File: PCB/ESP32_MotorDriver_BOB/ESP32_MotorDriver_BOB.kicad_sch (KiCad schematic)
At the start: 39 parts, among them J1 USB_C_Receptacle_USB2.0, J2 Conn_01x06, J3 Conn_01x06, J5 Conn_01x18, J6 Conn_01x07, Q1 SSM3J338R_LF, SW1 EN, SW2 BOOT, U1 ESP32-S2-SOLO-N4, U2 D3V3XA4B10LP, U4 TB6612FNG, U5 AP63203WU

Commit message: actual _v01
Issue with files being copied - these should be good
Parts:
- removed C1, C3, C5, C7: 10uF, Capacitor_SMD:C_0805_2012Metric_Pad1.18x1.45mm_HandSolder, symbol Device:C
- removed C10, C9: 22uF, Capacitor_SMD:C_0805_2012Metric_Pad1.18x1.45mm_HandSolder, symbol Device:C
- removed C2, C4, C6, C8: 100nF, Capacitor_SMD:C_0402_1005Metric_Pad0.74x0.62mm_HandSolder, symbol Device:C
- removed D1, D2: D_Schottky, Diode_SMD:D_SOD-323F, symbol Device:D_Schottky
- removed J1: USB_C_Receptacle_USB2.0, Connector_USB:USB_C_Receptacle_HRO_TYPE-C-31-M-12, symbol Connector:USB_C_Receptacle_USB2.0
- removed J2, J3: Conn_01x06, Connector_PinHeader_2.54mm:PinHeader_1x06_P2.54mm_Vertical, symbol Connector_Generic:Conn_01x06
- removed J5: Conn_01x18, Connector_PinHeader_2.54mm:PinHeader_1x18_P2.54mm_Vertical, symbol Connector_Generic:Conn_01x18
- removed L1: 4.7uH, Inductor_SMD:L_1008_2520Metric_Pad1.43x2.20mm_HandSolder, symbol Device:L_Small
- removed U1: ESP32-S2-SOLO-N4, ESP32_S2_SOLO_N4:XCVR_ESP32-S2-SOLO-N4, symbol ESP32-S2-SOLO-N4:ESP32-S2-SOLO-N4
- removed U2: D3V3XA4B10LP, Package_DFN_QFN:Diodes_UDFN-10_1x2.5mm_P0.5mm, symbol Power_Protection:D3V3XA4B10LP
- removed U4: TB6612FNG, Package_SO:SSOP-24_5.3x8.2mm_P0.65mm, symbol Driver_Motor:TB6612FNG
- removed U5: AP63203WU, Package_TO_SOT_SMD:TSOT-23-6, symbol Regulator_Switching:AP63203WU
- added C16: 100nF, Capacitor_SMD:C_0402_1005Metric_Pad0.74x0.62mm_HandSolder, symbol Device:C
- added D1: RED, LED_SMD:LED_1206_3216Metric_Pad1.42x1.75mm_HandSolder, symbol Device:LED
- added D2: GREEN, LED_SMD:LED_1206_3216Metric_Pad1.42x1.75mm_HandSolder, symbol Device:LED
- added D3: BLUE, LED_SMD:LED_1206_3216Metric_Pad1.42x1.75mm_HandSolder, symbol Device:LED
- added D4: YELLOW, LED_SMD:LED_1206_3216Metric_Pad1.42x1.75mm_HandSolder, symbol Device:LED
- added H1, H2, H3, H4: MountingHole, MountingHole:MountingHole_3.2mm_M3, symbol Mechanical:MountingHole
- added J10: Conn_01x07, Connector_PinSocket_2.54mm:PinSocket_1x07_P2.54mm_Vertical, symbol Connector_Generic:Conn_01x07
- added J11, J2: Conn_01x05, Connector_PinSocket_2.54mm:PinSocket_1x05_P2.54mm_Vertical, symbol Connector_Generic:Conn_01x05
- added J12, J4: Conn_01x06, Connector_PinSocket_2.54mm:PinSocket_1x06_P2.54mm_Vertical, symbol Connector_Generic:Conn_01x06
- added J13, J3: Conn_01x17, Connector_PinSocket_2.54mm:PinSocket_1x17_P2.54mm_Vertical, symbol Connector_Generic:Conn_01x17
- added J14: Conn_02x03_Odd_Even, Connector_PinHeader_2.54mm:PinHeader_2x03_P2.54mm_Vertical, symbol Connector_Generic:Conn_02x03_Odd_Even
- added J15: Conn_02x08_Odd_Even, Connector_PinHeader_2.54mm:PinHeader_2x08_P2.54mm_Vertical, symbol Connector_Generic:Conn_02x08_Odd_Even
- added J5, J6: Conn_01x06, Connector_JST:JST_XH_S6B-XH-A_1x06_P2.50mm_Horizontal, symbol Connector_Generic:Conn_01x06
- added J7: XT30, Connector_AMASS:AMASS_XT30PW-M_1x02_P2.50mm_Horizontal, symbol Connector:Conn_01x02_Pin
- added J8, J9: Conn_01x03, Connector_PinHeader_2.54mm:PinHeader_1x03_P2.54mm_Vertical, symbol Connector_Generic:Conn_01x03
- added R13, R14: 10k, Resistor_SMD:R_0402_1005Metric_Pad0.72x0.64mm_HandSolder, symbol Device:R
- added R5: 100k, Resistor_SMD:R_0402_1005Metric_Pad0.72x0.64mm_HandSolder, symbol Device:R
- added R6, R7, R8: 4k7, Resistor_SMD:R_0402_1005Metric_Pad0.72x0.64mm_HandSolder, symbol Device:R
- added U1: LDL1117S50R, Package_TO_SOT_SMD:SOT-223-3_TabPin2, symbol Regulator_Linear:LD1117S50TR_SOT223
- added U2: ER_OLEDM0.91_1x-I2C, Display:ER_OLEDM0.91_1x-I2C, symbol Display_Graphic:ER_OLEDM0.91_1x-I2C
- added U3: PCA9306D, Package_SO:SO-8_3.9x4.9mm_P1.27mm, symbol Interface:PCA9306D
- added U4: ESP32 MotorDriver BOB_v01, _silkscreen:logo_QUT, symbol _silkscreen:logo_qut
- C11: footprint Capacitor_SMD:C_0805_2012Metric_Pad1.18x1.45mm_HandSolder -> Capacitor_SMD:C_0402_1005Metric_Pad0.74x0.62mm_HandSolder; Manufacturer (none) -> Samsung Electro-Mechanics; PN_Digikey (none) -> 1276-CL05A106MP6NUN8CT-ND; PN_LCSC (none) -> C3902158; PN_Manufacturer (none) -> CL05A106MP6NUN8
- C12: Manufacturer (none) -> YAGEO; PN_Digikey (none) -> 311-3342-1-ND; PN_LCSC (none) -> C105882; PN_Manufacturer (none) -> CC0402KRX5R9BB104
- C13: value 100nF -> 10uF; LCSC PN C105882 -> C3902158; Manufacturer (none) -> Samsung Electro-Mechanics; PN_Digikey (none) -> 1276-CL05A106MP6NUN8CT-ND; PN_LCSC (none) -> C3902158; PN_Manufacturer (none) -> CL05A106MP6NUN8
- C14: value 100nF -> 10uF; LCSC PN (none) -> C3902158; Manufacturer (none) -> Samsung Electro-Mechanics; PN_Digikey (none) -> 1276-CL05A106MP6NUN8CT-ND; PN_LCSC (none) -> C3902158; PN_Manufacturer (none) -> CL05A106MP6NUN8
- C15: value 10uF -> 100nF; footprint Capacitor_SMD:C_0805_2012Metric_Pad1.18x1.45mm_HandSolder -> Capacitor_SMD:C_0402_1005Metric_Pad0.74x0.62mm_HandSolder; LCSC PN (none) -> C105882; Manufacturer (none) -> YAGEO; PN_Digikey (none) -> 311-3342-1-ND; PN_LCSC (none) -> C105882; PN_Manufacturer (none) -> CC0402KRX5R9BB104
- F1: footprint Fuse:Fuse_0805_2012Metric_Pad1.15x1.40mm_HandSolder -> digikey-footprints:0805; Manufacturer (none) -> Vishay
- J1: renamed from J6; footprint Connector_PinHeader_2.54mm:PinHeader_1x07_P2.54mm_Vertical -> Connector_PinSocket_2.54mm:PinSocket_1x07_P2.54mm_Vertical
- Q1: footprint SSM3J338R_LF:SOT-23F_TOS -> SSM3J338R:SOT-23F_TOS; Manufacturer (none) -> Toshiba Semiconductor and Storage
- R1, R2: value 5k1 -> 150R
- R10: value 4k7 -> 10k; LCSC PN (none) -> C851816; LCSC Part # C100047 -> (none); Manufacturer (none) -> YAGEO; PN_Digikey (none) -> YAG1249CT-ND; PN_LCSC (none) -> C851816; PN_Manufacturer (none) -> RC0402FR-0710KP
- R11, R12: LCSC PN C851816 -> (none)
- R3, R4: value 10k -> 150R; LCSC Part # C100047 -> (none)
- R9: LCSC Part # C100047 -> (none)
- SW1: value EN -> SW_Push; footprint _common:Switch SMD STO -> Button_Switch_SMD:SW_SPST_EVQP0; PN_Digikey 2508-R-667995CT-ND -> P12966SCT-ND; PN_Manufacturer R-667995 -> (none)
- SW2: value BOOT -> SW_Push; footprint _common:Switch SMD STO -> Button_Switch_SMD:SW_SPST_EVQP0; LCSC_PN C25168823 -> (none); PN_Digikey 2508-R-667995CT-ND -> P12966SCT-ND; PN_Manufacturer R-667995 -> (none)
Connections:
- net BOOT is gone; now on net GND: R4.2, SW2.1
- net EN is gone; now on net GND: R3.2, SW1.1
- net M01_STBY is gone; now on net IO8: R12.2
- net SCL is gone; now on net +3V3: R9.2
- net SDA is gone; now on an unnamed net: R10.2
- net +3V3: now also R11.2, J13.10 (Pin_10), J13.11 (Pin_11), J3.10 (Pin_10), J3.11 (Pin_11), J5.3 (Pin_3), J6.3 (Pin_3), R13.2, R8.2, U3.2 (VREF1); no longer C14.1, R10.1, R3.1, R4.1, R9.1
- net GND: now also C13.2, R1.2, R10.1, R2.2, C16.2, J10.1 (Pin_1), J12.6 (Pin_6), J13.1 (Pin_1), J13.17 (Pin_17), J14.1 (Pin_1), J15.10 (Pin_10), J15.12 (Pin_12), J15.14 (Pin_14), J15.16 (Pin_16), J15.2 (Pin_2), J15.4 (Pin_4), J15.6 (Pin_6), J15.8 (Pin_8), J3.1 (Pin_1), J3.17 (Pin_17), J4.6 (Pin_6), J5.6 (Pin_6), J6.6 (Pin_6), J7.1 (Pin_1), J8.1 (Pin_1), J9.1 (Pin_1), U1.1 (GND), U2.1 (GND), U3.1 (GND); no longer R1.1, R11.1, R12.1, R2.1, SW1.2, SW2.2
- net IO1: now also J13.2 (Pin_2), J3.2 (Pin_2), J8.3 (Pin_3)
- net IO15: now also J10.6 (Pin_6), J15.15 (Pin_15)
- net IO16: now also J10.7 (Pin_7), J15.13 (Pin_13)
- net IO17: now also J11.1 (Pin_1), J15.11 (Pin_11), J2.1 (Pin_1)
- net IO18: now also J11.2 (Pin_2), J15.9 (Pin_9), J2.2 (Pin_2)
- net IO2: now also J13.3 (Pin_3), J3.3 (Pin_3), J9.3 (Pin_3)
- net IO3: now also J11.4 (Pin_4), J2.4 (Pin_4), J5.4 (Pin_4)
- net IO39: now also J13.9 (Pin_9), J15.7 (Pin_7), J3.9 (Pin_9)
- net IO4: now also D1.2 (A), J10.2 (Pin_2)
- net IO40: now also J13.8 (Pin_8), J15.5 (Pin_5), J3.8 (Pin_8)
- net IO41: now also J13.7 (Pin_7), J15.3 (Pin_3), J3.7 (Pin_7)
- net IO42: now also J13.6 (Pin_6), J15.1 (Pin_1), J3.6 (Pin_6)
- net IO5: now also D2.2 (A), J10.3 (Pin_3)
- net IO6: now also D3.2 (A), J10.4 (Pin_4)
- net IO7: now also D4.2 (A), J10.5 (Pin_5)
- net IO8: now also C15.1, J11.3 (Pin_3), J2.3 (Pin_3)
- net IO9: now also J11.5 (Pin_5), J2.5 (Pin_5), J5.5 (Pin_5)
- net M1.1: now also J12.2 (Pin_2), J4.2 (Pin_2), J5.1 (Pin_1)
- net M1.2: now also J12.3 (Pin_3), J4.3 (Pin_3), J5.2 (Pin_2)
- net M2.1: now also J12.5 (Pin_5), J4.5 (Pin_5), J6.1 (Pin_1)
- net M2.2: now also J12.4 (Pin_4), J4.4 (Pin_4), J6.2 (Pin_2)
- net RXD: now also J13.5 (Pin_5), J14.3 (Pin_3), J3.5 (Pin_5)
- net TXD: now also J13.4 (Pin_4), J14.4 (Pin_4), J3.4 (Pin_4)
- net Vbatt: now also C11.1, C12.1, C13.1, F1.2, J12.1 (Pin_1), J4.1 (Pin_1), U1.3 (VI); no longer Q1.2
- net at Q1.1: no longer R11.2
- removed net VM: C11.1, C12.1, C15.1, F1.2
- new net: D2.1 (K), R2.1
- new net: D4.1 (K), R4.1
- new net: R13.1, R14.1, SW2.2
- new net: R11.1, R12.1, SW1.2
- new net: R5.1, U3.8 (EN)
- new net: D3.1 (K), R3.1
- new net: J7.2 (Pin_2), Q1.2
- new net: D1.1 (K), R1.1
- new net +5V: C14.1, J14.2 (Pin_2), J8.2 (Pin_2), J9.2 (Pin_2), R5.2, R6.2, R7.2, U1.2 (VO), U2.2 (VCC), U3.7 (VREF2)
- new net IO11: J13.16 (Pin_16), J3.16 (Pin_16), J6.4 (Pin_4)
- new net IO12: J13.15 (Pin_15), J3.15 (Pin_15), J6.5 (Pin_5)
- new net IO13: C16.1, J13.14 (Pin_14), J3.14 (Pin_14), R14.2
- new net IO33: J13.13 (Pin_13), J3.13 (Pin_13), R9.1, U3.3 (SCL1)
- new net IO34: J13.12 (Pin_12), J3.12 (Pin_12), R8.1, U3.4 (SDA1)
- new net SCL_5V0: J14.6 (Pin_6), R6.1, U2.3 (SCL), U3.6 (SCL2)
- new net SDA_5V0: J14.5 (Pin_5), R7.1, U2.4 (SDA), U3.5 (SDA2)
- no-connect marks 1 -> 0
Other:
- note added: "5V 1.2A for Servos etc"
- note added: "Battery Input and Protection"
- note added: "Four LEDs ( R, G, B, Y )"
- note added: "Header IOs for the ESP32"
- note added: "Header for all comms"
- note added: "I2C pull ups and level shift to 5V0"
- note added: "IO Mapping"
- note added: "Line Follower Strip IO"
- note added: "Most servos can take 3V3 PWM"
- note added: "Motor with encoder connecion via JST-XH"
- note added: "OLED on I2C"
- note added: "Second copy, 100mil away from the ESP32 for adding in wires etc"
- note added: "Switches with hardware debounce"
- note added: "Two Servo Connectors"
- note removed: "ESP32"
- note removed: "ESP32 Pin Swaps SPI.begin(sck, miso, mosi, cs); Wire.begin(I2C_SDA, I2C_SCL);"
- note removed: "Header IOs"
- note removed: "I2C"
- note removed: "Motor Driver"
- note removed: "Motor Power and Protection"
- note removed: "RESET and BOOT buttons"
- note removed: "Regulator Supply and 3V3"
- note removed: "USB C"
- moved on the sheet: J1

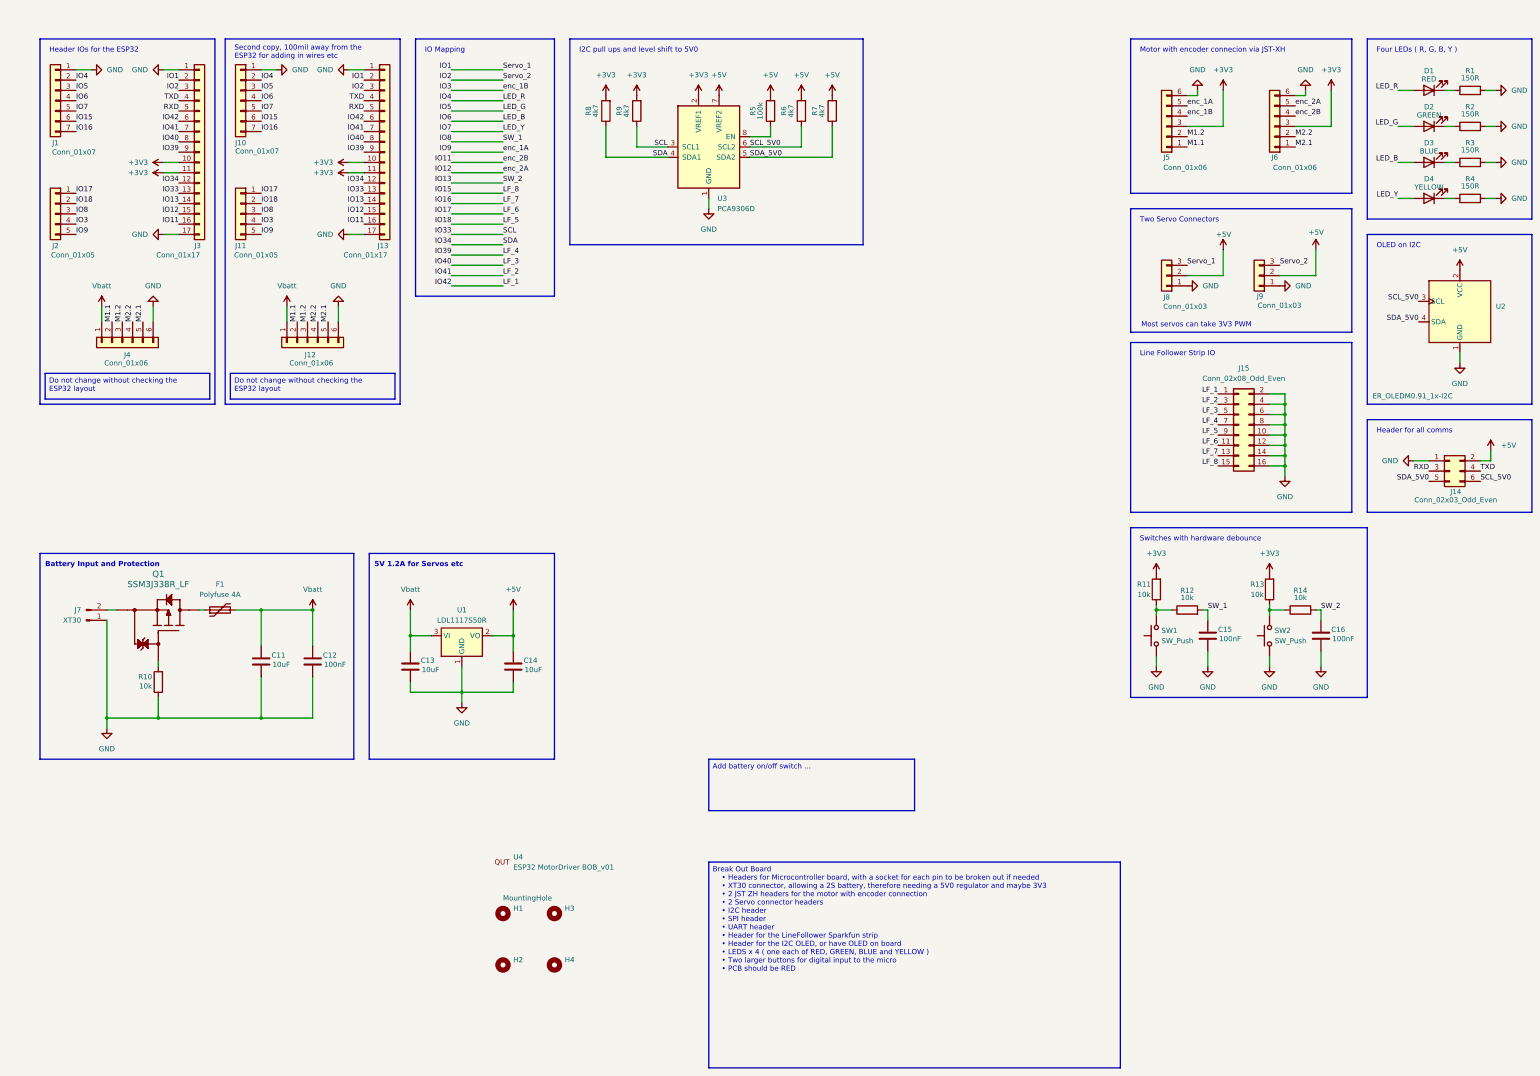
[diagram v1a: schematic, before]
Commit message: BOB v02
Submitted for manufacturer with a few minor fixes from v01. 3V3 to LineFollower array, New footprint for Motor connections and a switch added for power on/off
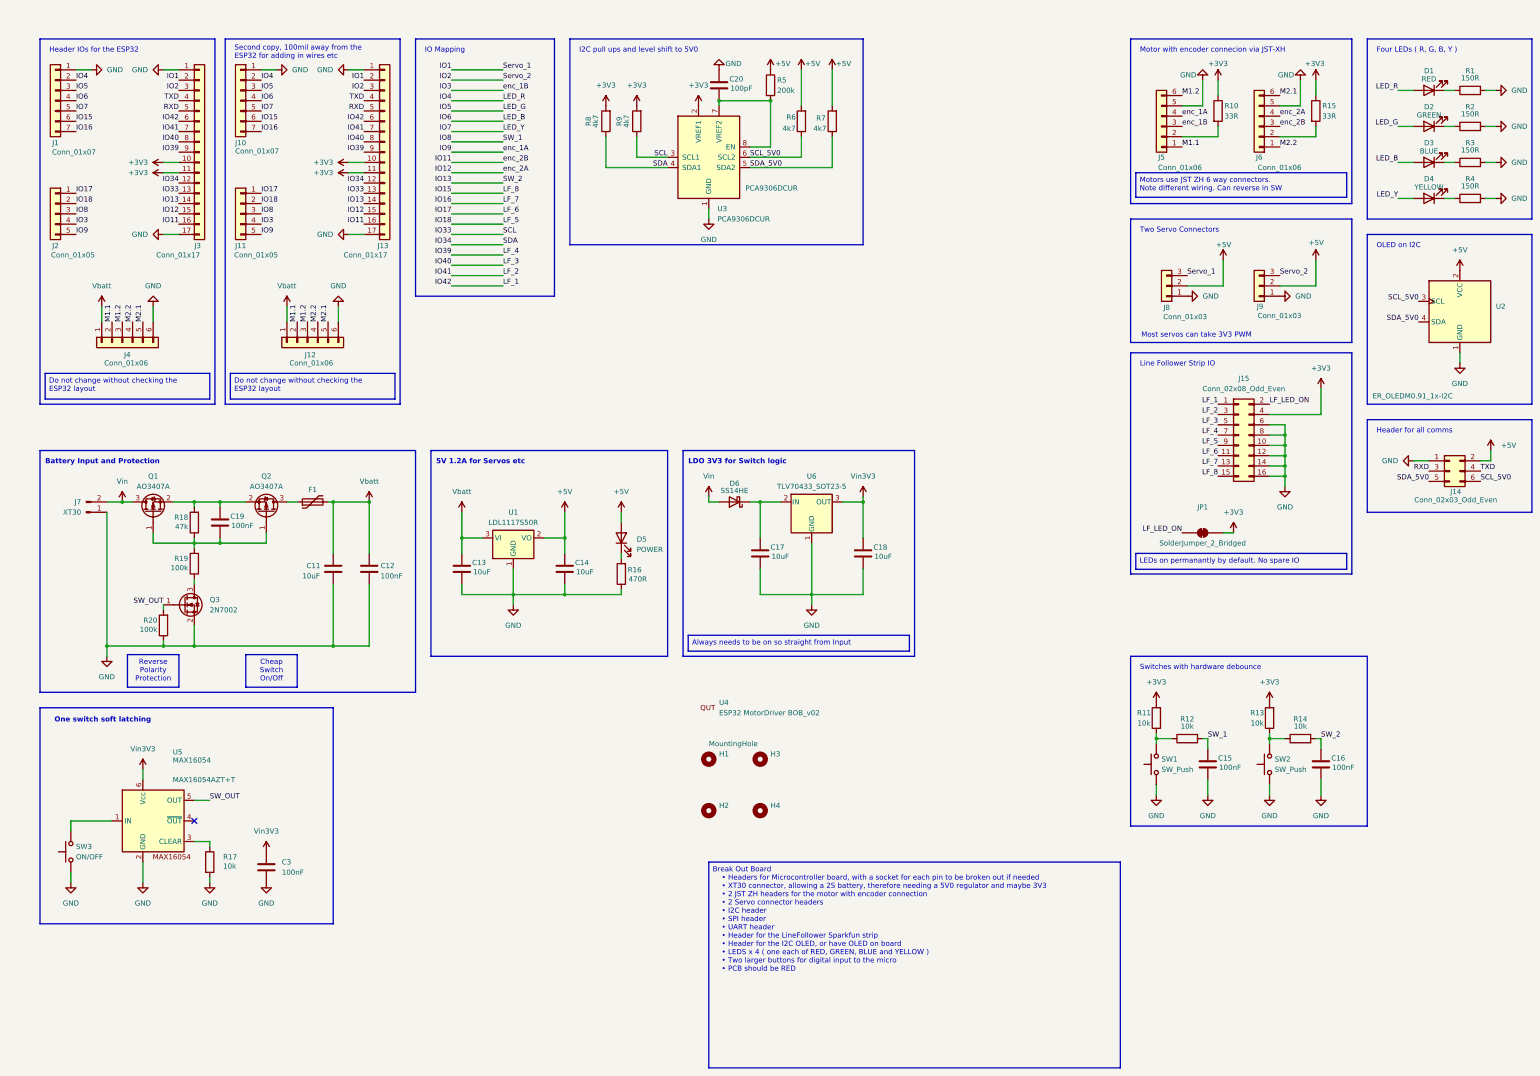
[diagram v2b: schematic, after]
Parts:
- removed Q1: SSM3J338R_LF, SSM3J338R:SOT-23F_TOS, symbol KiCADv6:SSM3J338R_LF
- removed U3: PCA9306D, Package_SO:SO-8_3.9x4.9mm_P1.27mm, symbol Interface:PCA9306D
- added C17, C18: 10uF, Capacitor_SMD:C_0805_2012Metric_Pad1.18x1.45mm_HandSolder, symbol Device:C
- added C19, C3: 100nF, Capacitor_SMD:C_0402_1005Metric_Pad0.74x0.62mm_HandSolder, symbol Device:C
- added C20: 100pF, Capacitor_SMD:C_0402_1005Metric_Pad0.74x0.62mm_HandSolder, symbol Device:C
- added D5: POWER, LED_SMD:LED_0805_2012Metric_Pad1.15x1.40mm_HandSolder, symbol Device:LED
- added D6: SS14HE, _diodes:D_SOD-323HE_SS14HE, symbol Device:D_Schottky
- added JP1: SolderJumper_2_Bridged, Jumper:SolderJumper-2_P1.3mm_Bridged_RoundedPad1.0x1.5mm, symbol Jumper:SolderJumper_2_Bridged
- added Q1, Q2: AO3407A, Package_TO_SOT_SMD:SOT-23, symbol Transistor_FET:AO3401A
- added Q3: 2N7002, Package_TO_SOT_SMD:SOT-23, symbol Transistor_FET:2N7002
- added R15: 33R, Resistor_SMD:R_0402_1005Metric_Pad0.72x0.64mm_HandSolder, symbol Device:R
- added R16: 470R, Resistor_SMD:R_0402_1005Metric_Pad0.72x0.64mm_HandSolder, symbol Device:R
- added R17: 10k, Resistor_SMD:R_0402_1005Metric_Pad0.72x0.64mm_HandSolder, symbol Device:R
- added R18: 47k, Resistor_SMD:R_0402_1005Metric_Pad0.72x0.64mm_HandSolder, symbol Device:R
- added R19, R20: 100k, Resistor_SMD:R_0402_1005Metric_Pad0.72x0.64mm_HandSolder, symbol Device:R
- added SW3: ON/OFF, Button_Switch_SMD:SW_SPST_EVQP0, symbol Switch:SW_Push
- added U3: PCA9306DCUR, Package_SO:VSSOP-8_3x3mm_P0.65mm, symbol Interface:PCA9306DC1
- added U5: MAX16054, Package_TO_SOT_SMD:SOT-23-6, symbol _ic_interface_switch:MAX16054
- added U6: TLV70433_SOT23-5, Package_TO_SOT_SMD:SOT-23-5, symbol _ic_power:TLV70433_SOT23-5
- C11, C13, C14: footprint Capacitor_SMD:C_0402_1005Metric_Pad0.74x0.62mm_HandSolder -> Capacitor_SMD:C_0805_2012Metric_Pad1.18x1.45mm_HandSolder; LCSC PN C3902158 -> (none); MANUFACTURER (none) -> Samsung Electro-Mechanics; Manufacturer Samsung Electro-Mechanics -> (none); PN_Digikey 1276-CL05A106MP6NUN8CT-ND -> 1276-2891-1-ND; PN_LCSC C3902158 -> C15850; PN_Manufacturer CL05A106MP6NUN8 -> CL21A106KAYNNNE
- C12, C15, C16: LCSC PN C105882 -> (none); MANUFACTURER (none) -> Murata Electronics; Manufacturer YAGEO -> (none); PN_Digikey 311-3342-1-ND -> 490-10700-1-ND; PN_LCSC C105882 -> C77020; PN_Manufacturer CC0402KRX5R9BB104 -> GRM155R71H104KE14D
- F1: value Polyfuse 4A -> PTC RESET FUSE 16V 2.5A 1812; footprint digikey-footprints:0805 -> Fuse:Fuse_1812_4532Metric_Pad1.30x3.40mm_HandSolder; LCSC PN C22368431 -> (none); MANUFACTURER (none) -> Bourns Inc.; Manufacturer Vishay -> (none); PN_Digikey MFU08054.00CT-ND -> MF-MSMF250/16X-2CT-ND; PN_LCSC C22368431 -> C210838; PN_Manufacturer MFU0805FF04000P100 -> MF-MSMF250/16X-2
- J5, J6: footprint Connector_JST:JST_XH_S6B-XH-A_1x06_P2.50mm_Horizontal -> Connector_JST:JST_ZH_S6B-ZR-SM4A-TF_1x06-1MP_P1.50mm_Horizontal; MANUFACTURER (none) -> JST Sales America Inc.; PN_Digikey (none) -> 455-S6B-ZR-ND; PN_LCSC (none) -> C20089292; PN_Manufacturer (none) -> S6B-ZR
- J7: LCSC PN C431092 -> (none); MANUFACTURER (none) -> Changzhou Amass Elec; Manufacturer Changzhou Amass Elec -> (none)
- R10: value 10k -> 33R; LCSC PN C851816 -> (none); Manufacturer YAGEO -> (none); PN_Digikey YAG1249CT-ND -> (none); PN_LCSC C851816 -> (none); PN_Manufacturer RC0402FR-0710KP -> (none)
- R5: value 100k -> 200k
- SW1, SW2: MANUFACTURER (none) -> Panasonic Industry; PN_LCSC (none) -> C6554563; PN_Manufacturer (none) -> EVQ-P0P02B
- U1: MANUFACTURER (none) -> STMicroelectronics; Manufacturer STMicroelectronics -> (none); PN_LCSC (none) -> C970558
- U4: value ESP32 MotorDriver BOB_v01 -> ESP32 MotorDriver BOB_v02; now left out of the parts list
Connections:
- net +3V3: now also J15.4 (Pin_4), R10.1, JP1.2 (B), R15.1, U3.2 (VREF1); no longer J5.3 (Pin_3), J6.3 (Pin_3)
- net +5V: now also R5.1, D5.2 (A); no longer R5.2
- net GND: now also J5.5 (Pin_5), J6.5 (Pin_5), C17.2, C18.2, C20.1, C3.2, Q3.2 (S), R16.1, R17.2, R20.1, SW3.1, U3.1 (GND), U5.2 (GND), U6.1 (GND); no longer J15.2 (Pin_2), J15.4 (Pin_4), J5.6 (Pin_6), J6.6 (Pin_6), R10.1
- net IO11: now also J6.3 (Pin_3); no longer J6.4 (Pin_4)
- net IO12: now also J6.4 (Pin_4); no longer J6.5 (Pin_5)
- net IO3: now also J5.3 (Pin_3); no longer J5.4 (Pin_4)
- net IO33: now also U3.3 (SCL1)
- net IO34: now also U3.4 (SDA1)
- net IO9: now also J5.4 (Pin_4); no longer J5.5 (Pin_5)
- net M1.2: now also J5.6 (Pin_6); no longer J5.2 (Pin_2)
- net M2.1: now also J6.6 (Pin_6); no longer J6.1 (Pin_1)
- net M2.2: now also J6.1 (Pin_1); no longer J6.2 (Pin_2)
- net SCL_5V0: now also U3.6 (SCL2)
- net SDA_5V0: now also U3.5 (SDA2)
- net Vin: now reaches J7.2 (Pin_2)
- net Vin: now also D6.2 (A), Q1.3 (D)
- net at R10.2: now also J5.2 (Pin_2)
- net at F1.1: now also Q2.3 (D)
- new net: C17.1, D6.1 (K), U6.2 (IN)
- new net: C20.2, R5.2, U3.7 (VREF2), U3.8 (EN)
- new net: C19.2, Q1.1 (G), Q2.1 (G), R18.1, R19.2
- new net: C19.1, Q1.2 (S), Q2.2 (S), R18.2
- new net: R17.1, U5.3 (CLEAR)
- new net: D5.1 (K), R16.2
- new net: Q3.3 (D), R19.1
- new net: J6.2 (Pin_2), R15.2
- new net: SW3.2, U5.1 (IN)
- new net LF_LED_ON: J15.2 (Pin_2), JP1.1 (A)
- new net SW_OUT: Q3.1 (G), R20.2, U5.5 (OUT)
- new net Vin3V3: C18.1, C3.1, U5.6 (Vcc), U6.3 (OUT)
- no-connect marks 0 -> 1
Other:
- note added: "LDO 3V3 for Switch logic"
- note added: "One switch soft latching"
- moved on the sheet: C11, C12, C13, C14, C15, C16, F1, H1, H2, H3, H4, J15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
